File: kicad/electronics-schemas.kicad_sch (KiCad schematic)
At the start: 1 part, among them P1 +12V

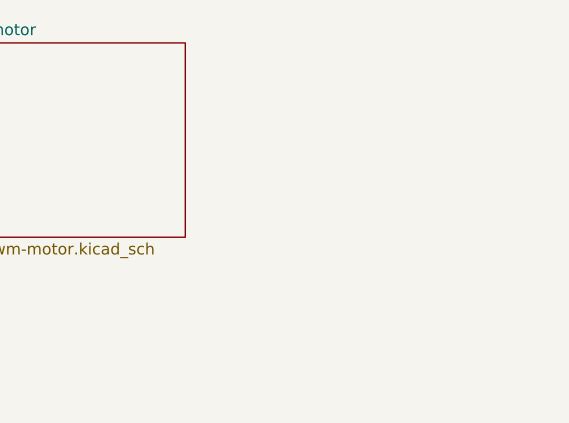
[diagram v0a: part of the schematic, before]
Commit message: Aggiunto ATMEGA328P
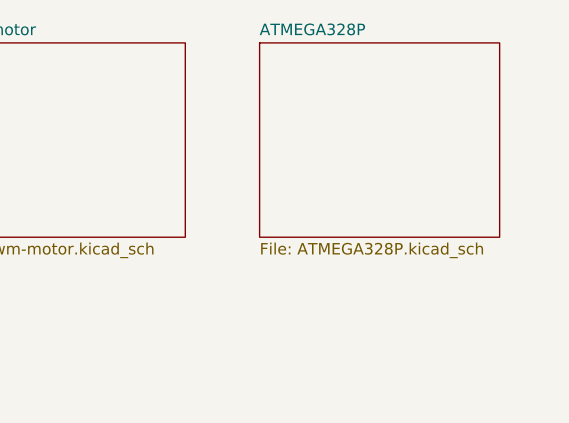
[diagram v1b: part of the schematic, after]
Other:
- added sheet ATMEGA328P (ATMEGA328P.kicad_sch)
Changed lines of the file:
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@@
+	)
+	(sheet
+		(at 225.425 21.59)
+		(size 26.67 21.59)
+		(exclude_from_sim no)
+		(in_bom yes)
+		(on_board yes)
+		(dnp no)
+		(fields_autoplaced yes)
+		(stroke
+			(width 0.1524)
+			(type solid)
+		)
+		(fill
+			(color 0 0 0 0.0000)
+		)
+		(property "Sheetname" "ATMEGA328P"
+			(at 225.425 20.8784 0)
+			(effects
+				(font
+					(size 1.27 1.27)
+				)
+				(justify left bottom)
+			)
+		)
+		(property "Sheetfile" "ATMEGA328P.kicad_sch"
+			(at 225.425 43.7646 0)
+			(effects
+				(font
+					(size 1.27 1.27)
+				)
+				(justify left top)
+			)
+		)
+		(instances
+			(project "electronics-schemas"
+				(path "/f1ade40e-ee4b-4e00-b57d-44850604005b"
+					(page "7")
+				)
+			)
+		)
 	)
 	(sheet
